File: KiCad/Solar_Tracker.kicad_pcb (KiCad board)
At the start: 2 copper layers, 130 parts, among them J1 +48V_IN, J10 HOLE, J11 HOLE, J12 HOLE, J13 HOLE, J14 ELJMP, J2 USB_OTG, J3 EL, J4 CONN_01X05, J5 CONN_02X03, J6 GPIO, J7 AZJMP, J8 AZ, J9 CONN_01X03, Q1 BUK9M42-60E, Q2 BUK9M42-60E, Q3 BUK9M42-60E, Q4 BUK9M42-60E, Q5 BUK9M42-60E, Q6 BUK9M42-60E, Q7 BUK9M42-60E, Q8 BUK9M42-60E, SW1 SWITCH, U1 MER1S4805SC, U11 75LBC182, U12 A4927, U2 A4927, U3 ATMEGA32U4-AU, U4 A4927, U5 A4927, U6 MER1S4805SC, Y1 16MHz

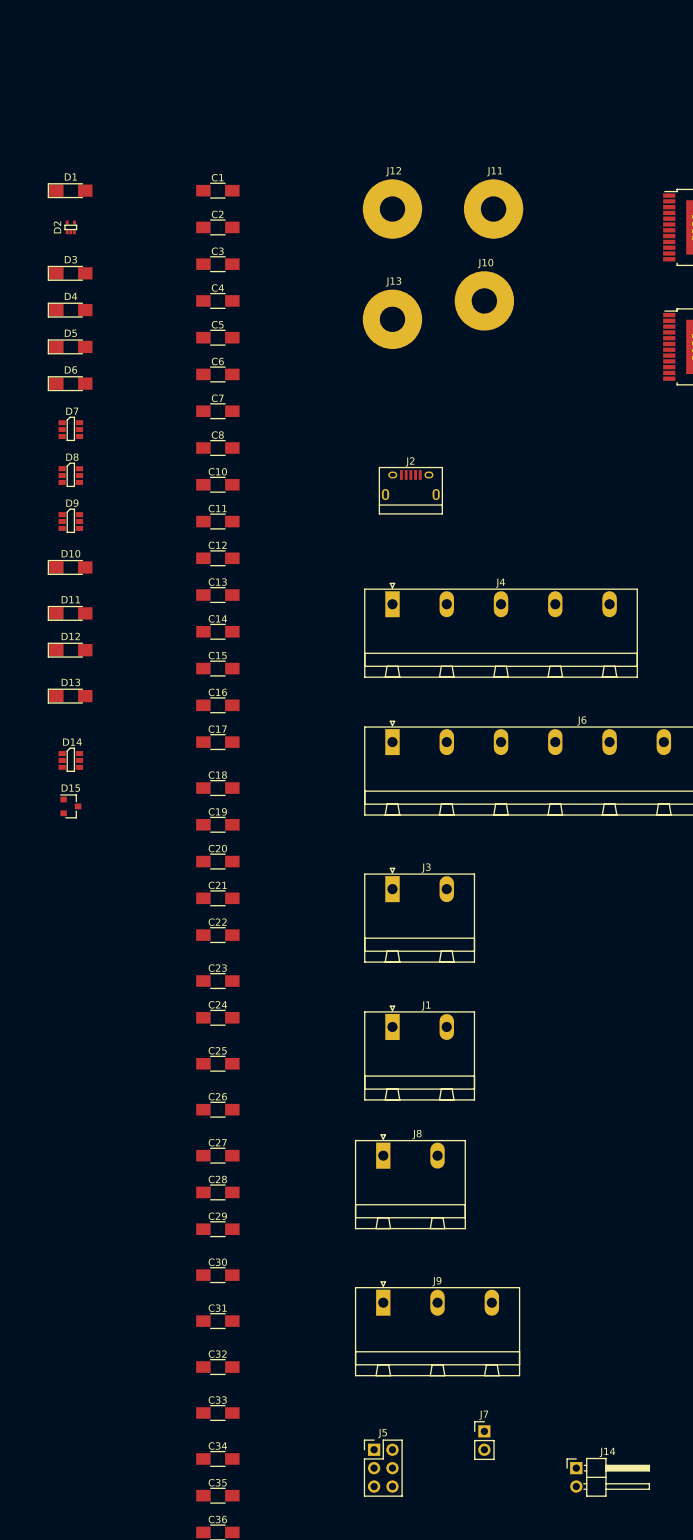
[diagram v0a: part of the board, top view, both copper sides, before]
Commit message: All components in PCB
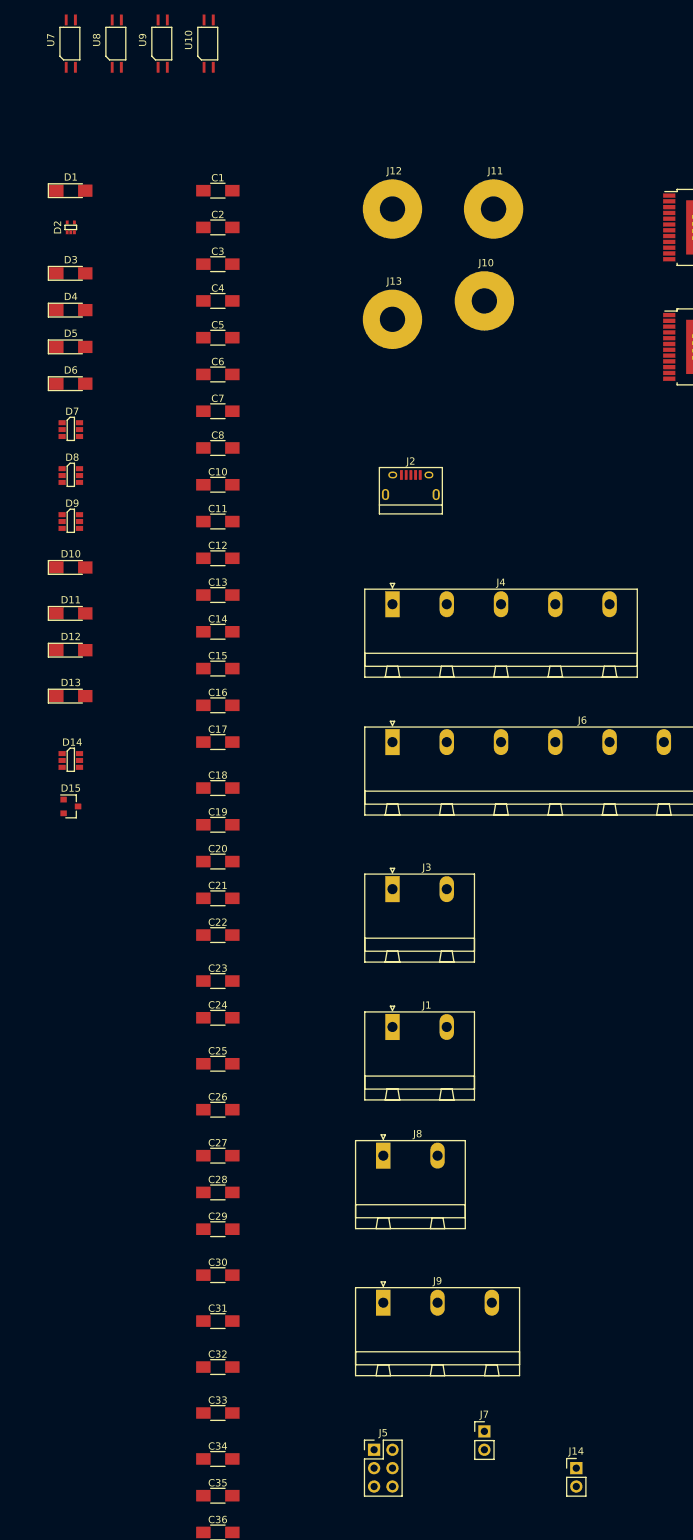
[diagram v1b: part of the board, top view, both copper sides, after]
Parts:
- added U10: TLP291, SOLAR_TRACKER:opto, F.Cu at (-6.35, -5.08)
- added U7: TLP291, SOLAR_TRACKER:opto, F.Cu at (-25.4, -5.08)
- added U8: TLP291, SOLAR_TRACKER:opto, F.Cu at (-19.1, -5.08)
- added U9: TLP291, SOLAR_TRACKER:opto, F.Cu at (-12.7, -5.08)
- J14: footprint Pin_Headers:Pin_Header_Angled_1x02_Pitch2.54mm -> Pin_Headers:Pin_Header_Straight_1x02_Pitch2.54mm

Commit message: Work on grouping components
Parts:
- moved R43 297.6 mm to (74.9, -30.5)
- moved R42 288.3 mm to (83.8, -20.3)
- moved R41 279.6 mm to (74.9, -20.3)
- moved R3 278.6 mm to (218.4, -14.0)
- moved R4 272.7 mm to (210.8, -19.1)
- moved R2 270.3 mm to (210.8, -14.0)
- moved D2 247.0 mm to (218.4, -19.1)
- moved R32 244.5 mm to (74.9, -25.4)
- moved C10 244.3 mm to (228.6, -15.2)
- moved C11 244.3 mm to (228.6, -10.2)
- moved C12 244.3 mm to (228.6, -5.08)
- moved C13 244.3 mm to (228.6, 0.00)
- moved C14 244.3 mm to (228.6, 5.08)
- moved R26 238.6 mm to (99.1, -33.0)
- moved C1 237.4 mm to (228.6, -26.7)
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
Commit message: saved changes
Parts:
- moved R44 448.7 mm to (295.9, -35.6)
- moved R35 398.8 mm to (264.2, -40.6)
- moved R36 398.8 mm to (264.2, -35.6)
- moved R37 398.8 mm to (264.2, -30.5)
- moved R38 398.8 mm to (264.2, -25.4)
- moved R39 398.8 mm to (264.2, -20.3)
- moved R40 398.8 mm to (264.2, -15.2)
- moved R34 382.0 mm to (271.8, -3.81)
- moved R16 373.9 mm to (295.9, -29.2)
- moved R17 373.9 mm to (295.9, -24.1)
- moved R28 367.0 mm to (256.5, -33.0)
- moved R29 367.0 mm to (256.5, -27.9)
- moved R30 367.0 mm to (256.5, -22.9)
- moved R31 367.0 mm to (256.5, -15.2)
- moved R33 353.9 mm to (245.1, 1.27)
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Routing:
- net Net-(D4-Pad1): track 0.00 -> 6.35 mm

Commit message: Started work on layout
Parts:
- moved J6 291.0 mm to (17.8, 30.5), turned to 270 degrees
- moved J5 285.8 mm to (17.8, -2.54)
- moved J9 246.9 mm to (74.9, 96.5)
- moved U11 242.1 mm to (58.4, 85.1)
- moved U10 241.0 mm to (50.8, 94.0), turned to 270 degrees
- moved R30 234.1 mm to (55.9, 97.8)
- moved U9 233.7 mm to (50.8, 90.2), turned to 270 degrees
- moved J4 232.0 mm to (78.7, 16.5), turned to 180 degrees
- moved R29 230.8 mm to (54.6, 83.8)
- moved D15 230.1 mm to (77.5, 88.9)
- moved R21 229.5 mm to (40.6, 90.2)
- moved R20 228.9 mm to (41.9, 85.1)
- moved R22 228.9 mm to (40.6, 94.0)
- moved U8 226.4 mm to (50.8, 86.4), turned to 90 degrees
- moved R35 226.2 mm to (73.7, 81.3), turned to 90 degrees
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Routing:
- net Net-(D4-Pad1): track 6.35 -> 0.00 mm
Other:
- board outline added: 119.4 x 87.6 mm

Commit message: more layout work
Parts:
- moved R13 198.1 mm to (304.8, 52.1), turned to 270 degrees
- moved R9 196.8 mm to (316.2, 43.2)
- moved C15 196.8 mm to (317.5, 22.9)
- moved C16 196.8 mm to (308.6, 22.9)
- moved C19 196.8 mm to (308.6, 27.9)
- moved D5 196.8 mm to (308.6, 43.2)
- moved R15 196.8 mm to (308.6, 33.0)
- moved Q3 192.5 mm to (304.8, 61.0), turned to 180 degrees
- moved R14 187.6 mm to (301.0, 52.1), turned to 270 degrees
- moved Q4 185.7 mm to (294.6, 52.1)
- moved U4 182.1 mm to (294.6, 63.5), turned to 90 degrees
- moved C18 178.0 mm to (285.8, 53.3), turned to 180 degrees
- moved C17 172.9 mm to (289.6, 39.4), turned to 180 degrees
- moved C4 47.1 mm to (268.0, 31.8)
- moved C3 39.6 mm to (268.0, 36.8)
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
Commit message: Layout updates
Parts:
- moved Q6 272.3 mm to (360.7, 57.1)
- moved Q5 258.9 mm to (354.3, 57.1)
- moved C20 251.7 mm to (341.6, 24.1)
- moved C21 251.7 mm to (350.5, 29.2)
- moved C22 251.7 mm to (350.5, 24.1)
- moved C23 251.7 mm to (341.6, 29.2)
- moved C24 251.7 mm to (350.5, 34.3)
- moved D10 251.7 mm to (341.6, 45.7)
- moved R18 251.7 mm to (350.5, 45.7)
- moved R19 251.7 mm to (341.6, 39.4)
- moved R24 251.7 mm to (350.5, 39.4)
- moved R26 251.7 mm to (341.6, 34.3)
- moved U5 251.7 mm to (345.4, 66.0)
- moved Q3 15.5 mm to (295.9, 48.3), turned to 90 degrees
- moved R13 5.08 mm to (299.7, 52.1)
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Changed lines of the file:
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@@
-(kicad_pcb (version 4) (host pcbnew 4.0.6)
+(kicad_pcb (version 4) (host pcbnew 4.0.7)
   (general
     (links 387)
     (no_connects 335)
-    (area 11.979 -64.935 445.845001 100.405001)
+    (area 5.805 -45.905 320.975001 108.595)
     (thickness 1.6)
     (drawings 3)
@@
     (pad_to_mask_clearance 0.2)
     (aux_axis_origin 0 0)
-    (visible_elements 7FFFF7FF)
+    (visible_elements 7FFEF7FF)
     (pcbplotparams
       (layerselection 0x00030_80000001)
@@
   )
   (module Capacitors_SMD:C_1206_HandSoldering (layer F.Cu)
-    (at 99.06 -43.18)
+    (at 341.63 24.13)
     (descr "Capacitor SMD 1206, hand soldering")
     (tags "capacitor 1206")
@@
   )
   (module Capacitors_SMD:C_1206_HandSoldering (layer F.Cu)
-    (at 107.95 -38.1)
+    (at 350.52 29.21)
     (descr "Capacitor SMD 1206, hand soldering")
     (tags "capacitor 1206")
@@
   )
   (module Capacitors_SMD:C_1206_HandSoldering (layer F.Cu)
-    (at 107.95 -43.18)
+    (at 350.52 24.13)
     (descr "Capacitor SMD 1206, hand soldering")
     (tags "capacitor 1206")
@@
   )
   (module Capacitors_SMD:C_1206_HandSoldering (layer F.Cu)
-    (at 99.06 -38.1)
+    (at 341.63 29.21)
     (descr "Capacitor SMD 1206, hand soldering")
     (tags "capacitor 1206")
@@
   )
   (module Capacitors_SMD:C_1206_HandSoldering (layer F.Cu)
-    (at 107.95 -33.02)
+    (at 350.52 34.29)
     (descr "Capacitor SMD 1206, hand soldering")
     (tags "capacitor 1206")
@@
   )
   (module LEDs:LED_1206_HandSoldering (layer F.Cu)
-    (at 99.06 -21.59)
+    (at 341.63 45.72)
     (descr "LED SMD 1206, hand soldering")
     (tags "LED 1206")
@@
   )
   (module Resistors_SMD:R_1206_HandSoldering (layer F.Cu)
-    (at 304.8 52.07 270)
+    (at 299.72 52.07 270)
     (descr "Resistor SMD 1206, hand soldering")
     (tags "resistor 1206")
@@
   )
   (module Resistors_SMD:R_1206_HandSoldering (layer F.Cu)
-    (at 300.99 52.07 270)
+    (at 297.18 52.07 270)
     (descr "Resistor SMD 1206, hand soldering")
     (tags "resistor 1206")
@@
   )
   (module Resistors_SMD:R_1206_HandSoldering (layer F.Cu)
-    (at 107.95 -21.59)
+    (at 350.52 45.72)
     (descr "Resistor SMD 1206, hand soldering")
     (tags "resistor 1206")
@@
   )
   (module Resistors_SMD:R_1206_HandSoldering (layer F.Cu)
-    (at 99.06 -27.94)
+    (at 341.63 39.37)
     (descr "Resistor SMD 1206, hand soldering")
     (tags "resistor 1206")
@@
   )
   (module Resistors_SMD:R_1206_HandSoldering (layer F.Cu)
-    (at 107.95 -27.94)
+    (at 350.52 39.37)
     (descr "Resistor SMD 1206, hand soldering")
     (tags "resistor 1206")
@@
   )
   (module Resistors_SMD:R_1206_HandSoldering (layer F.Cu)
-    (at 99.06 -33.02)
+    (at 341.63 34.29)
     (descr "Resistor SMD 1206, hand soldering")
     (tags "resistor 1206")
@@
   )
   (module Housings_SSOP:ST_PowerSSO-24_SlugDown_ThermalVias (layer F.Cu)
-    (at 102.87 -1.27)
+    (at 345.44 66.04)
     (descr "ST PowerSSO-24 1EP 7.5x10.3mm Pitch 0.8mm [JEDEC MO-271] (http://www.st.com/resource/en/datasheet/tda7266p.pdf, http://freedatasheets.com/downloads/Technical%20Note%20Powersso24%20TN0054.pdf)")
     (tags "ST PowerSSO-24 1EP 7.5x10.3mm Pitch 0.8mm")
@@
   )
   (module SOLAR_TRACKER:nFET (layer F.Cu)
-    (at 304.8 60.96 180)
-    (fp_text reference Q3 (at 4.43 1.35 270) (layer F.SilkS) hide
+    (at 295.91 48.26 90)
+    (fp_text reference Q3 (at 4.43 1.35 180) (layer F.SilkS) hide
       (effects (font (size 1 1) (thickness 0.15)))
     )
-    (fp_text value BUK9M42-60E (at -1.24 1.37 270) (layer F.Fab)
+    (fp_text value BUK9M42-60E (at -1.24 1.37 180) (layer F.Fab)
       (effects (font (size 1 1) (thickness 0.15)))
     )
@@
     (fp_line (start 3.4 0) (end 3.4 2.6) (layer F.SilkS) (width 0.15))
     (fp_line (start 3.4 2.6) (end 0 2.6) (layer F.SilkS) (width 0.15))
-    (pad 3 smd rect (at 2 3.1 180) (size 0.45 1) (layers F.Cu F.Paste F.Mask)
+    (pad 3 smd rect (at 2 3.1 90) (size 0.45 1) (layers F.Cu F.Paste F.Mask)
       (net 15 "Net-(C17-Pad2)"))
-    (pad 4 smd rect (at 2.65 3.1 180) (size 0.45 1) (layers F.Cu F.Paste F.Mask)
+    (pad 4 smd rect (at 2.65 3.1 90) (size 0.45 1) (layers F.Cu F.Paste F.Mask)
       (net 79 "Net-(Q3-Pad4)"))
-    (pad 2 smd rect (at 1.34 3.1 180) (size 0.45 1) (layers F.Cu F.Paste F.Mask)
+    (pad 2 smd rect (at 1.34 3.1 90) (size 0.45 1) (layers F.Cu F.Paste F.Mask)
       (net 15 "Net-(C17-Pad2)"))
-    (pad 1 smd rect (at 0.68 3.1 180) (size 0.45 1) (layers F.Cu F.Paste F.Mask)
+    (pad 1 smd rect (at 0.68 3.1 90) (size 0.45 1) (layers F.Cu F.Paste F.Mask)
       (net 15 "Net-(C17-Pad2)"))
-    (pad mb smd rect (at 1.67 -0.13 180) (size 2.45 5) (layers F.Cu F.Paste F.Mask)
+    (pad mb smd rect (at 1.67 -0.13 90) (size 2.45 5) (layers F.Cu F.Paste F.Mask)
       (net 16 EL_F))
   )
   (module SOLAR_TRACKER:nFET (layer F.Cu)
-    (at 294.64 52.07)
+    (at 292.1 52.07)
     (fp_text reference Q4 (at 4.43 1.35 90) (layer F.SilkS) hide
       (effects (font (size 1 1) (thickness 0.15)))
@@
   )
   (module SOLAR_TRACKER:nFET (layer F.Cu)
-    (at 105.41 -13.97)
+    (at 354.33 57.15)
     (fp_text reference Q5 (at 4.43 1.35 90) (layer F.SilkS) hide
       (effects (font (size 1 1) (thickness 0.15)))
@@
   )
   (module SOLAR_TRACKER:nFET (layer F.Cu)
-    (at 97.79 -13.97)
+    (at 360.68 57.15)
     (fp_text reference Q6 (at 4.43 1.35 90) (layer F.SilkS) hide
       (effects (font (size 1 1) (thickness 0.15)))

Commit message: Exported netlist
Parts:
- removed C33: 0.015u, Capacitors_SMD:C_1206_HandSoldering
- removed C34: 1000pF, Capacitors_SMD:C_1206_HandSoldering
- removed C35: 1u, Capacitors_SMD:C_1206_HandSoldering
- removed C36, C37: 0.1u, Capacitors_SMD:C_1206_HandSoldering
- removed D13: EL_FW, LEDs:LED_1206_HandSoldering
- removed D14: TVS_x4, SOLAR_TRACKER:tvs_quad
- removed D15: D_TVS_x2_AAC, TO_SOT_Packages_SMD:SOT-23
- removed J14: ELJMP, Pin_Headers:Pin_Header_Straight_1x02_Pitch2.54mm
- removed R42, R44: 150, Resistors_SMD:R_1206_HandSoldering
- removed R43: 1K, Resistors_SMD:R_1206_HandSoldering
- removed SW1: SWITCH, Buttons_Switches_SMD:SW_SPST_B3S-1000
- removed Y1: 16MHz, SOLAR_TRACKER:resonator
- C10: value 1u -> 10000u; footprint Capacitors_SMD:C_1206_HandSoldering -> SOLAR_TRACKER:vnd_cap
- C12: value 1u -> 0.1u
- C13: value 1u -> 100n
- C14: value 1u -> 0.015u
- C15, C20: value 1u -> 0.47u
- C16: value 0.1u -> 1u
- C17, C22: value 100n -> 0.1u
- C18: value 0.015u -> 100n
- C19: value 0.47u -> 0.015u
- C21: value 0.1u -> 10u
- C23: value 0.015u -> 100pF
- C24: value 0.47u -> 1u
- C25: value 10u -> 0.1u
- C26: value 0.47u -> 100pF
- C27: value 100pF -> 100n
- C28: value 1u -> 1000pF
- C29: value 0.1u -> 0.015u
- C30: value 100pF -> 1000pF
- C31: value 100n -> 1u
- C32: value 1000pF -> 0.47u
- C8: value 0.47u -> 0.1u
- C9: value 10000u -> 0.47u; footprint SOLAR_TRACKER:vnd_cap -> Capacitors_SMD:C_1206_HandSoldering
- D10: value EL_BW -> EL_FW
- D11: value RX -> +5V_ISO
- D12: value TX -> D_TVS_x2_AAC; footprint LEDs:LED_1206_HandSoldering -> TO_SOT_Packages_SMD:SOT-23
- D2: value TVS_USB -> +5V; footprint SOLAR_TRACKER:tvs_usb -> LEDs:LED_1206_HandSoldering
- D3: value +5V -> +48V
- D4: value +48V -> EL_FW
- D5: value EL_FW -> TVS_x4; footprint LEDs:LED_1206_HandSoldering -> SOLAR_TRACKER:tvs_quad
- D6: value +5V_ISO -> TVS_x4; footprint LEDs:LED_1206_HandSoldering -> SOLAR_TRACKER:tvs_quad
- D7: value TVS_x4 -> EL_BW; footprint SOLAR_TRACKER:tvs_quad -> LEDs:LED_1206_HandSoldering
- D8: value TVS_x4 -> RX; footprint SOLAR_TRACKER:tvs_quad -> LEDs:LED_1206_HandSoldering
- D9: value TVS_x4 -> TX; footprint SOLAR_TRACKER:tvs_quad -> LEDs:LED_1206_HandSoldering
- J10: value HOLE -> AZJMP; footprint SOLAR_TRACKER:M3 -> Pin_Headers:Pin_Header_Straight_1x02_Pitch2.54mm
- J11: value HOLE -> ELJMP; footprint SOLAR_TRACKER:M3 -> Pin_Headers:Pin_Header_Angled_1x02_Pitch2.54mm
- J12: value HOLE -> AZ; footprint SOLAR_TRACKER:M3 -> Connectors_Phoenix:PhoenixContact_GMSTBA-G_02x7.50mm_Angled
- J13: value HOLE -> CONN_01X03; footprint SOLAR_TRACKER:M3 -> Connectors_Phoenix:PhoenixContact_GMSTBA-G_03x7.50mm_Angled
- J2: value USB_OTG -> HOLE; footprint Connectors:USB_Micro-B -> SOLAR_TRACKER:M3
- J3: value EL -> HOLE; footprint Connectors_Phoenix:PhoenixContact_GMSTBA-G_02x7.50mm_Angled -> SOLAR_TRACKER:M3
- J4: value CONN_01X05 -> EL; footprint Connectors_Phoenix:PhoenixContact_GMSTBA-G_05x7.50mm_Angled -> Connectors_Phoenix:PhoenixContact_GMSTBA-G_02x7.50mm_Angled
- J5: value CONN_02X03 -> HOLE; footprint Pin_Headers:Pin_Header_Straight_2x03_Pitch2.54mm -> SOLAR_TRACKER:M3
- J6: value GPIO -> HOLE; footprint Connectors_Phoenix:PhoenixContact_GMSTBA-G_08x7.50mm_Angled -> SOLAR_TRACKER:M3
- J7: value AZJMP -> CONN_01X05; footprint Pin_Headers:Pin_Header_Straight_1x02_Pitch2.54mm -> Connectors_Phoenix:PhoenixContact_GMSTBA-G_05x7.50mm_Angled
- J8: value AZ -> GPIO
- J9: value CONN_01X03 -> GPIO; footprint Connectors_Phoenix:PhoenixContact_GMSTBA-G_03x7.50mm_Angled -> Connectors_Phoenix:PhoenixContact_GMSTBA-G_02x7.50mm_Angled
- R10, R11, R16, R17, R2, R20, R23, R26, R30, R31: value 1K -> 150
- R14, R18, R21, R24, R28, R29, R41, R8, R9: value 150 -> 1K
- R3: value 22 -> 150
- R4: value 22 -> 1K
- U3: value ATMEGA32U4-AU -> Nano; footprint Housings_QFP:TQFP-44_10x10mm_Pitch0.8mm -> SOLAR_TRACKER:nano
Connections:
- net PB7 renamed ELBL
- C1 pad 1: Net-(C1-Pad1) -> +5V
- C10 pad 1: +5V -> +48V
- C11 pad 1: +5V -> Net-(C11-Pad1)
- C12 pad 1: +5V -> +48V
- C13 pad 1: +5V -> +48V
- C13 pad 2: Earth -> Net-(C13-Pad2)
- C14 pad 1: +5V -> EL_F
- C14 pad 2: Earth -> Net-(C14-Pad2)
- C15 pad 2: Earth -> Net-(C15-Pad2)
- C16 pad 1: +48V -> Net-(C16-Pad1)
- C17 pad 2: Net-(C17-Pad2) -> Earth
- C18 pad 1: EL_F -> +48V
- C19 pad 1: Net-(C19-Pad1) -> AZ_B
- C20 pad 2: Earth -> Net-(C20-Pad2)
- C21 pad 1: +48V -> +5VD
- C21 pad 2: Earth -> GNDD
- C22 pad 1: +48V -> +5VD
- C22 pad 2: Net-(C22-Pad2) -> GNDD
- C23 pad 1: AZ_B -> Net-(C23-Pad1)
- C23 pad 2: Net-(C23-Pad2) -> GNDD
- C24 pad 2: Net-(C24-Pad2) -> Earth
- C25 pad 1: +5VD -> +48V
- C25 pad 2: GNDD -> Earth
- C26 pad 2: Net-(C26-Pad2) -> GNDD
- C27 pad 1: Net-(C27-Pad1) -> +48V
- C27 pad 2: GNDD -> Net-(C27-Pad2)
- C28 pad 1: Net-(C28-Pad1) -> Net-(C23-Pad1)
- C29 pad 1: +48V -> AZ_F
- C29 pad 2: Earth -> Net-(C29-Pad2)
- C30 pad 1: Net-(C30-Pad1) -> Net-(C26-Pad1)
- C30 pad 2: GNDD -> Earth
- C31 pad 1: +48V -> GNDD
- C31 pad 2: Net-(C31-Pad2) -> Earth
- C32 pad 1: Net-(C27-Pad1) -> Net-(C32-Pad1)
- C32 pad 2: Earth -> Net-(C32-Pad2)
- C8 pad 1: Net-(C8-Pad1) -> +5V
- C8 pad 2: Net-(C8-Pad2) -> Earth
- C9 pad 1: +48V -> Net-(C9-Pad1)
- C9 pad 2: Earth -> Net-(C9-Pad2)
- D10 pad 2: Net-(C22-Pad2) -> Net-(C27-Pad2)
- D11 pad 2: E2 -> +5VD
- D12 pad 1: Net-(D12-Pad1) -> Net-(C23-Pad1)
- D12 pad 2: E6 -> Net-(C26-Pad1)
- D2 pad 2: Net-(D2-Pad2) -> +5V
- D3 pad 2: +5V -> +48V
- D4 pad 2: +48V -> Net-(C13-Pad2)
- D5 pad 1: Net-(D5-Pad1) -> A1
- D5 pad 2: Net-(C17-Pad2) -> Earth
- D6 pad 1: Net-(D6-Pad1) -> C3
- D6 pad 2: +5VD -> Earth
- D7 pad 1: A1 -> Net-(D7-Pad1)
- D7 pad 2: Earth -> Net-(C18-Pad2)
- D8 pad 1: RESET -> Net-(D8-Pad1)
- D8 pad 2: Earth -> RLED
- D9 pad 1: D7 -> Net-(D9-Pad1)
- D9 pad 2: Earth -> TLED
- J10 pad 1: Earth -> AZRTE
- J11 pad 1: Earth -> ELRTE
- J12 pad 1: Earth -> AZ_F
- J13 pad 1: Earth -> Net-(C26-Pad1)
- J2 pad 1: +5V -> Earth
- J3 pad 1: EL_F -> Earth
- J4 pad 1: Net-(J4-Pad1) -> EL_F
- J4 pad 2: A0 -> EL_B
- J5 pad 1: MISO -> Earth
- J6 pad 1: D4 -> Earth
- J7 pad 1: AZRTE -> Net-(J7-Pad1)
- J7 pad 2: Earth -> A0
- J8 pad 1: AZ_F -> C0
- J8 pad 2: AZ_B -> C1
- J9 pad 1: Net-(C30-Pad1) -> C2
- J9 pad 2: Net-(C27-Pad1) -> C3
- Q3 pad 1: Net-(C17-Pad2) -> Net-(C13-Pad2)
- Q3 pad 2: Net-(C17-Pad2) -> Net-(C13-Pad2)
- Q3 pad 3: Net-(C17-Pad2) -> Net-(C13-Pad2)
- Q5 pad 1: Net-(C22-Pad2) -> Net-(C18-Pad2)
- Q5 pad 2: Net-(C22-Pad2) -> Net-(C18-Pad2)
- Q5 pad 3: Net-(C22-Pad2) -> Net-(C18-Pad2)
- Q7 pad 1: Net-(C31-Pad2) -> Net-(C27-Pad2)
- Q7 pad 2: Net-(C31-Pad2) -> Net-(C27-Pad2)
- Q7 pad 3: Net-(C31-Pad2) -> Net-(C27-Pad2)
- R10 pad 1: Net-(D4-Pad1) -> Net-(Q3-Pad4)
- R11 pad 1: Net-(R10-Pad2) -> Net-(Q4-Pad4)
- R12 pad 1: Net-(R11-Pad2) -> +48V
- R12 pad 2: Earth -> Net-(R12-Pad2)
- R13 pad 1: Net-(Q3-Pad4) -> Net-(J7-Pad1)
- R13 pad 2: Net-(R13-Pad2) -> +5V
- R14 pad 1: Net-(Q4-Pad4) -> ELRTE
- R14 pad 2: Net-(R14-Pad2) -> +5V
- R15 pad 1: +48V -> AZRTE
- R15 pad 2: Net-(R15-Pad2) -> +5V
- R16 pad 1: ELRTE -> Net-(D7-Pad1)
- R16 pad 2: +5V -> Earth
- R17 pad 1: AZRTE -> Net-(Q5-Pad4)
- R17 pad 2: +5V -> Net-(R17-Pad2)
- R18 pad 1: Net-(D10-Pad1) -> +5V
- R18 pad 2: Earth -> RX
- R19 pad 1: Net-(Q5-Pad4) -> EN
- R2 pad 1: +5V -> Net-(Q1-Pad4)
- R2 pad 2: RESET -> Net-(R2-Pad2)
- R20 pad 1: +5V -> TX
- R20 pad 2: RX -> Net-(R20-Pad2)
- R21 pad 1: EN -> +5V
- R21 pad 2: Net-(R21-Pad2) -> ISO_PWR_DET
- R22 pad 1: TX -> Net-(Q6-Pad4)
- R23 pad 1: +5V -> Net-(D8-Pad1)
- R23 pad 2: ISO_PWR_DET -> Earth
- R24 pad 1: Net-(Q6-Pad4) -> +48V
- R25 pad 1: Net-(D11-Pad1) -> Net-(D9-Pad1)
- R26 pad 1: +48V -> +5VD
- R27 pad 1: Net-(D12-Pad1) -> Net-(R27-Pad1)
- R27 pad 2: Earth -> Net-(R27-Pad2)
- R29 pad 1: Net-(R29-Pad1) -> +5VD
- R3 pad 1: Net-(D2-Pad1) -> Net-(Q2-Pad4)
- R30 pad 1: +5VD -> Net-(D10-Pad1)
- R30 pad 2: Net-(R30-Pad2) -> Earth
- R31 pad 1: +5VD -> Net-(D11-Pad1)
- R31 pad 2: Net-(R31-Pad2) -> GNDD
- R32 pad 1: Net-(D13-Pad1) -> Net-(C26-Pad1)
- R32 pad 2: Earth -> Net-(C23-Pad1)
- R33 pad 1: Net-(D6-Pad1) -> +5VD
- R33 pad 2: GNDD -> Net-(R33-Pad2)
- R34 pad 1: Net-(C30-Pad1) -> Net-(R33-Pad2)
- R34 pad 2: Net-(C27-Pad1) -> Net-(R34-Pad2)
- R35 pad 1: +5VD -> Net-(R34-Pad2)
- R35 pad 2: Net-(R35-Pad2) -> Net-(C26-Pad1)
- R36 pad 1: Net-(R35-Pad2) -> Net-(C23-Pad1)
- R37 pad 2: Net-(C30-Pad1) -> Net-(R37-Pad2)
- R38 pad 1: Net-(C27-Pad1) -> Net-(R37-Pad2)
- R38 pad 2: Net-(R38-Pad2) -> GNDD
- R39 pad 1: Net-(R38-Pad2) -> Net-(Q7-Pad4)
- R4 pad 1: Net-(R4-Pad1) -> +48V
- R4 pad 2: Net-(D2-Pad2) -> Net-(R4-Pad2)
- R40 pad 1: Net-(R39-Pad2) -> Net-(Q8-Pad4)
- R40 pad 2: GNDD -> Net-(R40-Pad2)
- R41 pad 1: Net-(Q7-Pad4) -> +48V
- R5 pad 1: Net-(Q1-Pad4) -> Net-(D2-Pad1)
- R5 pad 2: Net-(R5-Pad2) -> Earth
- R6 pad 1: Net-(Q2-Pad4) -> Net-(D4-Pad1)
- R6 pad 2: Net-(R6-Pad2) -> Earth
- R7 pad 1: +48V -> Net-(D3-Pad1)
- R8 pad 1: Net-(D3-Pad1) -> Net-(R7-Pad2)
- R8 pad 2: Earth -> Net-(R8-Pad2)
- R9 pad 1: Net-(D5-Pad1) -> Net-(R8-Pad2)
- U10 pad 1: Net-(R22-Pad2) -> Net-(R20-Pad2)
- U10 pad 4: Net-(R31-Pad2) -> Net-(R29-Pad2)
- U11 pad 1: Net-(R29-Pad2) -> Net-(R27-Pad2)
- U11 pad 2: Net-(R30-Pad2) -> Net-(R28-Pad2)
- U11 pad 3: Net-(R30-Pad2) -> Net-(R28-Pad2)
- U11 pad 4: Net-(R31-Pad2) -> Net-(R29-Pad2)
- U11 pad 6: Net-(C30-Pad1) -> Net-(C26-Pad1)
- U11 pad 7: Net-(C27-Pad1) -> Net-(C23-Pad1)
- U12 pad 15: Net-(C31-Pad2) -> Net-(C27-Pad2)
- U12 pad 16: Net-(R41-Pad2) -> Net-(R39-Pad2)
- U12 pad 17: Net-(R42-Pad2) -> Net-(R40-Pad2)
- U12 pad 19: Net-(C33-Pad2) -> Net-(C29-Pad2)
- U12 pad 20: Net-(C28-Pad1) -> Net-(C24-Pad1)
- U12 pad 21: Net-(C26-Pad1) -> Net-(C32-Pad1)
- U12 pad 22: Net-(C26-Pad2) -> Net-(C32-Pad2)
- U12 pad 3: Net-(R43-Pad2) -> Net-(R41-Pad2)
- U12 pad 4: Net-(R43-Pad2) -> Net-(R41-Pad2)
- U12 pad 5: PB0 -> AZFH
- U12 pad 6: PB1 -> AZFL
- U2 pad 16: Net-(R5-Pad2) -> Net-(R2-Pad2)
- U2 pad 17: Net-(R6-Pad2) -> Net-(R3-Pad2)
- U2 pad 21: Net-(C8-Pad1) -> Net-(C9-Pad1)
- U2 pad 22: Net-(C8-Pad2) -> Net-(C9-Pad2)
- U2 pad 3: Net-(R7-Pad2) -> Net-(R4-Pad2)
- U2 pad 4: Net-(R7-Pad2) -> Net-(R4-Pad2)
- U2 pad 5: PB6 -> ELBH
- U3 pad 1: E6 -> TX
- U3 pad 10: MOSI -> ISO_PWR_DET
- U3 pad 11: MISO -> ELBH
- U3 pad 13: RESET -> ELFH
- U3 pad 14: +5V -> ELFL
- U3 pad 15: Earth -> AZRTE
- U3 pad 16: Net-(U3-Pad16) -> ELRTE
- U3 pad 18: EN -> Net-(C2-Pad1)
- U3 pad 19: ISO_PWR_DET -> C0
- U3 pad 2: +5V -> RX
- U3 pad 20: RX -> C1
- U3 pad 21: TX -> C2
- U3 pad 22: D5 -> C3
- U3 pad 23: Earth -> TLED
- U3 pad 24: +5V -> RLED
- U3 pad 25: D4 -> A6
- U3 pad 26: D6 -> A7
- U3 pad 27: D7 -> Net-(U3-Pad27)
- U3 pad 28: PB4 -> Net-(U3-Pad28)
- U3 pad 29: PB5 -> Earth
- U3 pad 3: Net-(R4-Pad1) -> Net-(U3-Pad3)
- U3 pad 30: PB6 -> +5V
- U3 pad 4: Net-(R3-Pad2) -> Earth
- U3 pad 5: Earth -> AZBH
- U3 pad 6: Net-(C1-Pad1) -> AZBL
- U3 pad 7: +5V -> AZFH
- U3 pad 8: PB0 -> AZFL
- U3 pad 9: PB1 -> EN
- U4 pad 15: Net-(C17-Pad2) -> Net-(C13-Pad2)
- U4 pad 16: Net-(R13-Pad2) -> Net-(R10-Pad2)
- U4 pad 17: Net-(R14-Pad2) -> Net-(R11-Pad2)
- U4 pad 19: Net-(C18-Pad2) -> Net-(C14-Pad2)
- U4 pad 20: Net-(C15-Pad1) -> Net-(C11-Pad1)
- U4 pad 21: Net-(C19-Pad1) -> Net-(C15-Pad1)
- U4 pad 22: Net-(C19-Pad2) -> Net-(C15-Pad2)
- U4 pad 3: Net-(R15-Pad2) -> Net-(R12-Pad2)
- U4 pad 4: Net-(R15-Pad2) -> Net-(R12-Pad2)
- U4 pad 5: PB4 -> ELFH
- U4 pad 6: PB5 -> ELFL
- U5 pad 15: Net-(C22-Pad2) -> Net-(C18-Pad2)
- U5 pad 16: Net-(R19-Pad2) -> Net-(R17-Pad2)
- U5 pad 17: Net-(R24-Pad2) -> Net-(R22-Pad2)
- U5 pad 19: Net-(C23-Pad2) -> Net-(C19-Pad2)
- U5 pad 20: Net-(C20-Pad1) -> Net-(C16-Pad1)
- U5 pad 21: Net-(C24-Pad1) -> Net-(C20-Pad1)
- U5 pad 22: Net-(C24-Pad2) -> Net-(C20-Pad2)
- U5 pad 3: Net-(R26-Pad2) -> Net-(R24-Pad2)
- U5 pad 4: Net-(R26-Pad2) -> Net-(R24-Pad2)
- U5 pad 5: MOSI -> AZBH
- U5 pad 6: MISO -> AZBL
- U7 pad 1: Net-(R28-Pad2) -> Net-(R26-Pad2)
- U8 pad 1: Net-(R29-Pad1) -> Net-(R27-Pad1)
- U9 pad 1: Net-(R21-Pad2) -> Net-(R19-Pad2)
- U9 pad 4: Net-(R30-Pad2) -> Net-(R28-Pad2)
